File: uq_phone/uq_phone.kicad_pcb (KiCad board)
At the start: 4 copper layers, 116.9 x 105 mm, 304 parts, among them J1 USB4105-GF-A, J10 SJ-3551B-MSMT-TR-67, J11 Conn_01x02, J2 S3B-PH-SM4-TB_LF__SN_, J3 20279-001E-03, J4 20279-001E-03, J6 Conn_ARM_SWD_TagConnect_TC2030, J7 Conn_01x02, J8 KP15B-6S-SF_800_, J9 541324562, M1 VCDM0834B004L, Q1 MMBT3904LP-7, Q2 MMBT3904LP-7, SW1 SKTAAAE010, SW10 SKTAAAE010, SW11 SKTAAAE010, SW12 SKTAAAE010, SW13 SKTAAAE010, SW14 SKTAAAE010, SW15 SKTAAAE010, SW16 SKTAAAE010, SW17 SKTAAAE010, SW18 SKTAAAE010, SW19 SKTAAAE010, SW2 SKTAAAE010, SW20 SKTAAAE010, SW21 SKTAAAE010, SW22 SKTAAAE010, SW23 SKTAAAE010, SW24 SKTAAAE010, SW25 SKTAAAE010, SW26 SKTAAAE010, SW27 SKTAAAE010, SW28 SKTAAAE010, SW29 SKTAAAE010, SW3 SKTAAAE010, SW30 SKTAAAE010, SW31 SKTAAAE010, SW32 SKTAAAE010, SW33 SKTAAAE010, SW34 SKTAAAE010, SW35 SKTAAAE010, SW36 SKTAAAE010, SW37 SKTAAAE010, SW38 SKTAAAE010, SW39 SKTAAAE010, SW4 SKTAAAE010, SW40 SKTAAAE010, SW41 SKTAAAE010, SW42 SKTAAAE010, SW43 SKSCLCE010, SW44 SKSCLCE010, SW45 SKSCLCE010, SW46 SKSCLCE010, SW5 SKTAAAE010, SW6 SKTAAAE010, SW7 SKTAAAE010, SW8 SKTAAAE010, SW9 SKTAAAE010, U1 MCP73871-2CCI_ML, U10 TPD3F303DQDR, U11 TPD8F003DQDR, U12 MCP1664T-E/OT, U13 TS3A5018RSVR, U14 NAU88C22YG, U2 TPS62162DSGR, U3 BQ27441DRZR-G1A, U4 RC7620_1104625, U5 TXB0108RGYR, U6 TXB0108RGYR, U7 STM32H730VBTx, U8 LSM6DSVTR, U9 DRV2603RUNR

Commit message: Update Keypad
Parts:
- removed the LED13 at (137.1, 131.7)
- removed the LED13 at (169.8, 167.5)
- removed the LED13 at (180.2, 146.2)
- removed the LED13 at (137.1, 123.4)
- removed the LED13 at (155.3, 130.7)
- removed the LED13 at (158.5, 167.5)
- removed the LED13 at (180.2, 153.5)
- removed the LED13 at (124.0, 126.8)
- removed the LED13 at (180.2, 167.5)
- removed the LED13 at (170.2, 134.5)
- removed the LED13 at (183.3, 138.7)
- removed the LED13 at (158.5, 160.2)
- removed the LED13 at (137.2, 165.9)
- removed the LED13 at (109.3, 123.2)
- removed the LED13 at (155.3, 138.9)
- removed the LED13 at (169.8, 160.2)
- removed the LED13 at (183.3, 130.4)
- removed the LED13 at (169.8, 153.5)
- removed the LED13 at (158.5, 153.5)
- removed the LED13 at (169.8, 146.2)
- removed the LED13 at (109.3, 131.4)
- removed the LED13 at (180.2, 160.2)
- removed the LED13 at (158.5, 146.2)
- removed the REF** at (110.5, 157.0)
- removed the REF** at (124.0, 165.5)
- removed the REF** at (137.5, 140.0)
- removed the REF** at (137.5, 165.5)
- removed the REF** at (124.0, 157.0)
- removed the REF** at (110.5, 148.5)
- removed the REF** at (124.0, 148.4)
- removed the REF** at (124.0, 140.0)
- removed the REF** at (110.5, 140.0)
- removed the REF** at (137.5, 148.4)
- removed the REF** at (110.5, 165.5)
- removed the REF** at (137.5, 157.0)
- removed SW26, SW28, SW30, SW32: SKTAAAE010, custom_footprints:SKTAAAE010
- removed the SW36 at (174.2, 141.0)
- removed the SW36 at (136.2, 132.8)
- removed the SW36 at (169.3, 140.9)
- removed the SW36 at (179.4, 157.6)
- removed the SW36 at (136.2, 129.0)
- removed the SW36 at (136.2, 124.5)
- removed the SW36 at (108.5, 132.5)
- removed the SW36 at (128.0, 133.3)
- removed the SW36 at (179.4, 161.3)
- removed the SW36 at (179.4, 164.8)
- removed the SW36 at (176.3, 133.6)
- removed the SW36 at (164.0, 133.5)
- removed the SW36 at (123.0, 128.0)
- removed the SW36 at (169.2, 135.6)
- removed the SW36 at (108.5, 120.5)
- removed the SW36 at (157.7, 154.6)
- removed the SW36 at (179.4, 143.6)
- removed the SW36 at (117.8, 125.8)
- removed the SW36 at (168.9, 154.6)
- removed the SW36 at (169.2, 131.8)
- removed the SW36 at (123.0, 133.2)
- removed the SW36 at (157.7, 143.6)
- removed the SW36 at (154.5, 131.8)
- removed the SW36 at (179.4, 147.3)
- removed the SW36 at (154.5, 136.2)
- removed the SW36 at (154.5, 128.0)
- removed the SW36 at (157.7, 147.3)
- removed the SW36 at (108.5, 128.8)
- removed the SW36 at (127.5, 120.8)
- removed the SW36 at (123.0, 120.8)
- removed the SW36 at (168.9, 161.3)
- removed the SW36 at (182.5, 136.0)
- removed the SW36 at (234.2, 138.1)
- removed the SW36 at (157.7, 168.6)
- removed the SW36 at (157.7, 164.8)
- removed the SW36 at (157.7, 150.8)
- removed the SW36 at (108.5, 124.2)
- removed the SW36 at (179.4, 150.8)
- removed the SW36 at (136.2, 120.8)
- removed the SW36 at (157.7, 157.6)
- removed the SW36 at (179.4, 168.6)
- removed the SW36 at (130.1, 125.9)
- removed the SW36 at (168.9, 150.8)
- removed the SW36 at (168.9, 164.8)
- removed the SW36 at (168.9, 147.3)
- removed the SW36 at (163.8, 138.1)
- removed the SW36 at (169.3, 128.4)
- removed the SW36 at (179.4, 154.6)
- removed the SW36 at (130.1, 130.2)
- removed the SW36 at (123.0, 124.2)
- removed the SW36 at (182.5, 127.8)
- removed the SW36 at (176.3, 137.8)
- removed the SW36 at (168.9, 157.6)
- removed the SW36 at (154.5, 140.0)
- removed the SW36 at (157.7, 161.3)
- removed the SW36 at (117.6, 130.4)
- removed the SW36 at (168.9, 143.6)
- removed the SW36 at (173.8, 128.4)
- removed the SW36 at (182.5, 131.5)
- removed the SW36 at (168.9, 168.6)
- removed the SW36 at (182.5, 139.8)
- removed SW46: SKSCLCE010, custom_footprints:SKSCLCE010
- added REF**: 8.5mmSnaptron, custom_footprints:8.5mmSnaptron, F.Cu at (160.4, 143.4)
- added REF**: 8.5mmSnaptron, custom_footprints:8.5mmSnaptron, F.Cu at (127.5, 143.4)
- added REF**: 8.5mmSnaptron, custom_footprints:8.5mmSnaptron, F.Cu at (127.5, 159.4)
- added REF**: 8.5mmSnaptron, custom_footprints:8.5mmSnaptron, F.Cu at (127.5, 167.4)
- added REF**: 8.5mmSnaptron, custom_footprints:8.5mmSnaptron, F.Cu at (160.4, 167.4)
- added REF**: 8.5mmSnaptron, custom_footprints:8.5mmSnaptron, F.Cu at (160.4, 159.4)
- added REF**: 8.5mmSnaptron, custom_footprints:8.5mmSnaptron, F.Cu at (144.6, 167.4)
- added REF**: 8.5mmSnaptron, custom_footprints:8.5mmSnaptron, F.Cu at (144.6, 151.4)
- added REF**: 8.5mmSnaptron, custom_footprints:8.5mmSnaptron, F.Cu at (144.6, 159.4)
- added REF**: 8.5mmSnaptron, custom_footprints:8.5mmSnaptron, F.Cu at (144.6, 143.4)
- added REF**: 8.5mmSnaptron, custom_footprints:8.5mmSnaptron, F.Cu at (160.4, 151.4)
- added REF**: 8.5mmSnaptron, custom_footprints:8.5mmSnaptron, F.Cu at (127.5, 151.4)
- added SW36: SKTAAAE010, custom_footprints:SKTAAAE010, F.Cu at (81.3, 132.8)
- moved SW40 157.9 mm to (81.3, 139.8)
- moved SW39 157.7 mm to (81.3, 135.8)
- moved SW35 151.2 mm to (81.3, 128.8)
- moved SW8 148.1 mm to (83.3, 161.6)
- moved R48 146.0 mm to (67.1, 128.4), turned to -90 degrees
- moved SW2 145.5 mm to (83.3, 168.6)
- moved SW1 145.1 mm to (83.3, 164.6)
- moved SW20 143.1 mm to (83.3, 147.6)
- moved SW19 142.9 mm to (83.3, 143.6)
- moved SW31 141.0 mm to (95.3, 140.4)
- moved SW22 140.4 mm to (95.3, 147.6)
- moved SW25 140.0 mm to (90.0, 135.9), turned to 90 degrees
- moved SW14 139.4 mm to (83.3, 154.6)
- moved SW13 139.2 mm to (83.3, 150.6)
- moved SW34 138.4 mm to (95.3, 136.2)
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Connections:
- SW1 pad 1: Net-(SW1-Pad1) -> PB_STAR
- SW1 pad 2: Net-(SW1-Pad2) -> GND
- SW1 pad 3: Net-(SW1-Pad1) -> PB_STAR
- SW1 pad 4: Net-(SW1-Pad2) -> GND
- SW10 pad 1: Net-(SW10-Pad1) -> PB_2
- SW10 pad 2: Net-(SW10-Pad2) -> GND
- SW10 pad 3: Net-(SW10-Pad1) -> PB_2
- SW10 pad 4: Net-(SW10-Pad2) -> GND
- SW11 pad 1: Net-(SW11-Pad1) -> PB_3
- SW11 pad 2: Net-(SW11-Pad2) -> GND
- SW11 pad 3: Net-(SW11-Pad1) -> PB_3
- SW11 pad 4: Net-(SW11-Pad2) -> GND
- SW12 pad 1: Net-(SW11-Pad1) -> PB_3
- SW12 pad 2: Net-(SW11-Pad2) -> GND
- SW12 pad 3: Net-(SW11-Pad1) -> PB_3
- SW12 pad 4: Net-(SW11-Pad2) -> GND
- SW13 pad 1: Net-(SW13-Pad1) -> PB_4
- SW13 pad 2: Net-(SW13-Pad2) -> GND
- SW13 pad 3: Net-(SW13-Pad1) -> PB_4
- SW13 pad 4: Net-(SW13-Pad2) -> GND
- SW14 pad 1: Net-(SW13-Pad1) -> PB_4
- SW14 pad 2: Net-(SW13-Pad2) -> GND
- SW14 pad 3: Net-(SW13-Pad1) -> PB_4
- SW14 pad 4: Net-(SW13-Pad2) -> GND
- SW15 pad 1: Net-(SW15-Pad1) -> PB_5
- SW15 pad 2: Net-(SW15-Pad2) -> GND
- SW15 pad 3: Net-(SW15-Pad1) -> PB_5
- SW15 pad 4: Net-(SW15-Pad2) -> GND
- SW16 pad 1: Net-(SW15-Pad1) -> PB_5
- SW16 pad 2: Net-(SW15-Pad2) -> GND
- SW16 pad 3: Net-(SW15-Pad1) -> PB_5
- SW16 pad 4: Net-(SW15-Pad2) -> GND
- SW17 pad 1: Net-(SW17-Pad1) -> PB_6
- SW17 pad 2: Net-(SW17-Pad2) -> GND
- SW17 pad 3: Net-(SW17-Pad1) -> PB_6
- SW17 pad 4: Net-(SW17-Pad2) -> GND
- SW18 pad 1: Net-(SW17-Pad1) -> PB_6
- SW18 pad 2: Net-(SW17-Pad2) -> GND
- SW18 pad 3: Net-(SW17-Pad1) -> PB_6
- SW18 pad 4: Net-(SW17-Pad2) -> GND
- SW19 pad 1: Net-(SW19-Pad1) -> PB_7
- SW19 pad 2: Net-(SW19-Pad2) -> GND
- SW19 pad 3: Net-(SW19-Pad1) -> PB_7
- SW19 pad 4: Net-(SW19-Pad2) -> GND
- SW2 pad 1: Net-(SW1-Pad1) -> PB_STAR
- SW2 pad 2: Net-(SW1-Pad2) -> GND
- SW2 pad 3: Net-(SW1-Pad1) -> PB_STAR
- SW2 pad 4: Net-(SW1-Pad2) -> GND
- SW20 pad 1: Net-(SW19-Pad1) -> PB_7
- SW20 pad 2: Net-(SW19-Pad2) -> GND
- SW20 pad 3: Net-(SW19-Pad1) -> PB_7
- SW20 pad 4: Net-(SW19-Pad2) -> GND
- SW21 pad 1: Net-(SW21-Pad1) -> PB_8
- SW21 pad 2: Net-(SW21-Pad2) -> GND
- SW21 pad 3: Net-(SW21-Pad1) -> PB_8
- SW21 pad 4: Net-(SW21-Pad2) -> GND
- SW22 pad 1: Net-(SW21-Pad1) -> PB_8
- SW22 pad 2: Net-(SW21-Pad2) -> GND
- SW22 pad 3: Net-(SW21-Pad1) -> PB_8
- SW22 pad 4: Net-(SW21-Pad2) -> GND
- SW23 pad 1: Net-(SW23-Pad1) -> PB_9
- SW23 pad 2: Net-(SW23-Pad2) -> GND
- SW23 pad 3: Net-(SW23-Pad1) -> PB_9
- SW23 pad 4: Net-(SW23-Pad2) -> GND
- SW24 pad 1: Net-(SW23-Pad1) -> PB_9
- SW24 pad 2: Net-(SW23-Pad2) -> GND
- SW24 pad 3: Net-(SW23-Pad1) -> PB_9
- SW24 pad 4: Net-(SW23-Pad2) -> GND
- SW25 pad 1: Net-(SW25-Pad1) -> PB_DPAD_LEFT
- SW25 pad 2: Net-(SW25-Pad2) -> GND
- SW25 pad 3: Net-(SW25-Pad1) -> PB_DPAD_LEFT
- SW25 pad 4: Net-(SW25-Pad2) -> GND
- SW27 pad 1: Net-(SW27-Pad1) -> PB_DPAD_UP
- SW27 pad 2: Net-(SW27-Pad2) -> GND
- SW27 pad 3: Net-(SW27-Pad1) -> PB_DPAD_UP
- SW27 pad 4: Net-(SW27-Pad2) -> GND
- SW29 pad 1: Net-(SW29-Pad1) -> PB_DPAD_RIGHT
- SW29 pad 2: Net-(SW29-Pad2) -> GND
- SW29 pad 3: Net-(SW29-Pad1) -> PB_DPAD_RIGHT
- SW29 pad 4: Net-(SW29-Pad2) -> GND
- SW3 pad 1: Net-(SW3-Pad1) -> PB_0
- SW3 pad 2: Net-(SW3-Pad2) -> GND
- SW3 pad 3: Net-(SW3-Pad1) -> PB_0
- SW3 pad 4: Net-(SW3-Pad2) -> GND
- SW31 pad 1: Net-(SW31-Pad1) -> PB_DPAD_DOWN
- SW31 pad 2: Net-(SW31-Pad2) -> GND
- SW31 pad 3: Net-(SW31-Pad1) -> PB_DPAD_DOWN
- SW31 pad 4: Net-(SW31-Pad2) -> GND
- SW33 pad 1: Net-(SW33-Pad1) -> PB_DPAD_SELECT
- SW33 pad 2: Net-(SW33-Pad2) -> GND
- SW33 pad 3: Net-(SW33-Pad1) -> PB_DPAD_SELECT
- SW33 pad 4: Net-(SW33-Pad2) -> GND
- SW34 pad 1: Net-(SW33-Pad1) -> PB_DPAD_SELECT
- SW34 pad 2: Net-(SW33-Pad2) -> GND
- SW34 pad 3: Net-(SW33-Pad1) -> PB_DPAD_SELECT
- SW34 pad 4: Net-(SW33-Pad2) -> GND
- SW35 pad 1: Net-(SW35-Pad1) -> PB_MENU_L
- SW35 pad 2: Net-(SW35-Pad2) -> GND
- SW35 pad 3: Net-(SW35-Pad1) -> PB_MENU_L
- SW35 pad 4: Net-(SW35-Pad2) -> GND
- SW37 pad 1: Net-(SW37-Pad1) -> PB_MENU_R
- SW37 pad 2: Net-(SW37-Pad2) -> GND
- SW37 pad 3: Net-(SW37-Pad1) -> PB_MENU_R
- SW37 pad 4: Net-(SW37-Pad2) -> GND
- SW38 pad 1: Net-(SW37-Pad1) -> PB_MENU_R
- SW38 pad 2: Net-(SW37-Pad2) -> GND
- SW38 pad 3: Net-(SW37-Pad1) -> PB_MENU_R
- SW38 pad 4: Net-(SW37-Pad2) -> GND
- SW39 pad 1: Net-(SW39-Pad1) -> PB_CALL
- SW39 pad 2: Net-(SW39-Pad2) -> GND
- SW39 pad 3: Net-(SW39-Pad1) -> PB_CALL
- SW39 pad 4: Net-(SW39-Pad2) -> GND
- SW4 pad 1: Net-(SW3-Pad1) -> PB_0
- SW4 pad 2: Net-(SW3-Pad2) -> GND
- SW4 pad 3: Net-(SW3-Pad1) -> PB_0
- SW4 pad 4: Net-(SW3-Pad2) -> GND
- SW40 pad 1: Net-(SW39-Pad1) -> PB_CALL
- SW40 pad 2: Net-(SW39-Pad2) -> GND
- SW40 pad 3: Net-(SW39-Pad1) -> PB_CALL
- SW40 pad 4: Net-(SW39-Pad2) -> GND
- SW41 pad 1: Net-(SW41-Pad1) -> PB_END_CALL
- SW41 pad 2: Net-(SW41-Pad2) -> GND
- SW41 pad 3: Net-(SW41-Pad1) -> PB_END_CALL
- SW41 pad 4: Net-(SW41-Pad2) -> GND
- SW42 pad 1: Net-(SW41-Pad1) -> PB_END_CALL
- SW42 pad 2: Net-(SW41-Pad2) -> GND
- SW42 pad 3: Net-(SW41-Pad1) -> PB_END_CALL
- SW42 pad 4: Net-(SW41-Pad2) -> GND
- SW43 pad 1: unconnected-(SW43-Pad1) -> PB_VOL_UP
- SW43 pad 2: unconnected-(SW43-Pad2) -> PB_VOL_UP
- SW43 pad 3: unconnected-(SW43-Pad3) -> GND
- SW43 pad 4: unconnected-(SW43-Pad4) -> GND
- SW44 pad 1: unconnected-(SW44-Pad1) -> PB_PWR
- SW44 pad 2: unconnected-(SW44-Pad2) -> PB_PWR
- SW44 pad 3: unconnected-(SW44-Pad3) -> GND
- SW44 pad 4: unconnected-(SW44-Pad4) -> GND
- SW45 pad 1: unconnected-(SW45-Pad1) -> PB_VOL_DOWN
- SW45 pad 2: unconnected-(SW45-Pad2) -> PB_VOL_DOWN
- SW45 pad 3: unconnected-(SW45-Pad3) -> GND
- SW45 pad 4: unconnected-(SW45-Pad4) -> GND
- SW5 pad 1: Net-(SW5-Pad1) -> PB_HASH
- SW5 pad 2: Net-(SW5-Pad2) -> GND
- SW5 pad 3: Net-(SW5-Pad1) -> PB_HASH
- SW5 pad 4: Net-(SW5-Pad2) -> GND
- SW6 pad 1: Net-(SW5-Pad1) -> PB_HASH
- SW6 pad 2: Net-(SW5-Pad2) -> GND
- SW6 pad 3: Net-(SW5-Pad1) -> PB_HASH
- SW6 pad 4: Net-(SW5-Pad2) -> GND
- SW7 pad 1: Net-(SW7-Pad1) -> PB_1
- SW7 pad 2: Net-(SW7-Pad2) -> GND
- SW7 pad 3: Net-(SW7-Pad1) -> PB_1
- SW7 pad 4: Net-(SW7-Pad2) -> GND
- SW8 pad 1: Net-(SW7-Pad1) -> PB_1
- SW8 pad 2: Net-(SW7-Pad2) -> GND
- SW8 pad 3: Net-(SW7-Pad1) -> PB_1
- SW8 pad 4: Net-(SW7-Pad2) -> GND
- SW9 pad 1: Net-(SW10-Pad1) -> PB_2
- SW9 pad 2: Net-(SW10-Pad2) -> GND
- SW9 pad 3: Net-(SW10-Pad1) -> PB_2
- SW9 pad 4: Net-(SW10-Pad2) -> GND
- U7 pad 1: unconnected-(U7-PE2-Pad1) -> PB_HASH
- U7 pad 12: unconnected-(U7-PH0-Pad12) -> PB_8
- U7 pad 13: unconnected-(U7-PH1-Pad13) -> PB_9
- U7 pad 15: unconnected-(U7-PC0-Pad15) -> PB_MENU_L
- U7 pad 16: unconnected-(U7-PC1-Pad16) -> PB_MENU_R
- U7 pad 2: unconnected-(U7-PE3-Pad2) -> PB_1
- U7 pad 22: unconnected-(U7-PA0-Pad22) -> PB_PWR
- U7 pad 23: unconnected-(U7-PA1-Pad23) -> PB_VOL_DOWN
- U7 pad 24: unconnected-(U7-PA2-Pad24) -> PB_VOL_UP
- U7 pad 25: unconnected-(U7-PA3-Pad25) -> LED_DATA
- U7 pad 3: unconnected-(U7-PE4-Pad3) -> PB_2
- U7 pad 4: unconnected-(U7-PE5-Pad4) -> PB_3
- U7 pad 5: unconnected-(U7-PE6-Pad5) -> PB_4
- U7 pad 7: unconnected-(U7-PC13-Pad7) -> PB_5
- U7 pad 77: unconnected-(U7-PA15(JTDI)-Pad77) -> PB_END_CALL
- U7 pad 8: unconnected-(U7-PC14-Pad8) -> PB_6
- U7 pad 87: unconnected-(U7-PD6-Pad87) -> PB_CALL
- U7 pad 89: unconnected-(U7-PB3(JTDO-Pad89) -> PB_DPAD_UP
- U7 pad 9: unconnected-(U7-PC15-Pad9) -> PB_7
- U7 pad 90: unconnected-(U7-PB4(NJTRST)-Pad90) -> PB_DPAD_DOWN
- U7 pad 91: unconnected-(U7-PB5-Pad91) -> PB_DPAD_RIGHT
- U7 pad 92: unconnected-(U7-PB6-Pad92) -> PB_DPAD_LEFT
- U7 pad 93: unconnected-(U7-PB7-Pad93) -> PB_DPAD_SELECT
- U7 pad 97: unconnected-(U7-PE0-Pad97) -> PB_STAR
- U7 pad 98: unconnected-(U7-PE1-Pad98) -> PB_0
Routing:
- net (no net): track 9.00 -> 0.00 mm
- net PB_STAR: track 0.00 -> 1.50 mm
- net PB_MENU_R: track 0.00 -> 1.50 mm
- net PB_MENU_L: track 0.00 -> 1.50 mm
- net PB_HASH: track 0.00 -> 1.50 mm
- net PB_END_CALL: track 0.00 -> 1.50 mm
- net PB_DPAD_SELECT: track 0.00 -> 1.50 mm
- net PB_CALL: track 0.00 -> 1.50 mm
- net PB_9: track 0.00 -> 1.50 mm
- net PB_8: track 0.00 -> 1.50 mm
- net PB_7: track 0.00 -> 1.50 mm
- net PB_6: track 0.00 -> 1.50 mm
- net PB_5: track 0.00 -> 1.50 mm
- net PB_4: track 0.00 -> 1.50 mm
- net PB_3: track 0.00 -> 1.50 mm
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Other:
- board size 116.9 x 105 mm -> 138 x 104.1 mm
- board text added: "LEFT"
- board text added: "RIGHT"

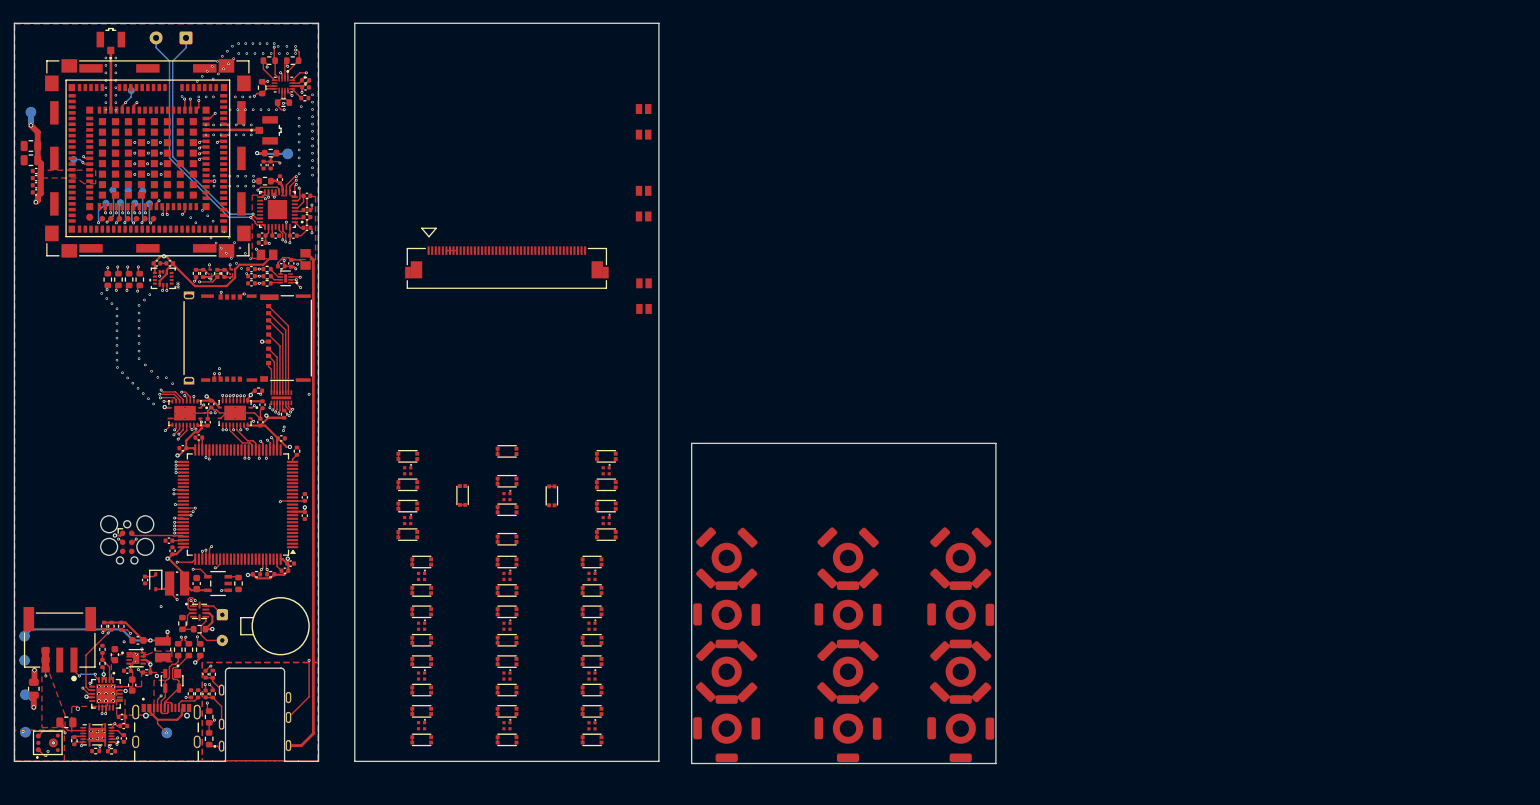
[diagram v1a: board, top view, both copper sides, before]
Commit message: Add Front Pannel Suboard and connector
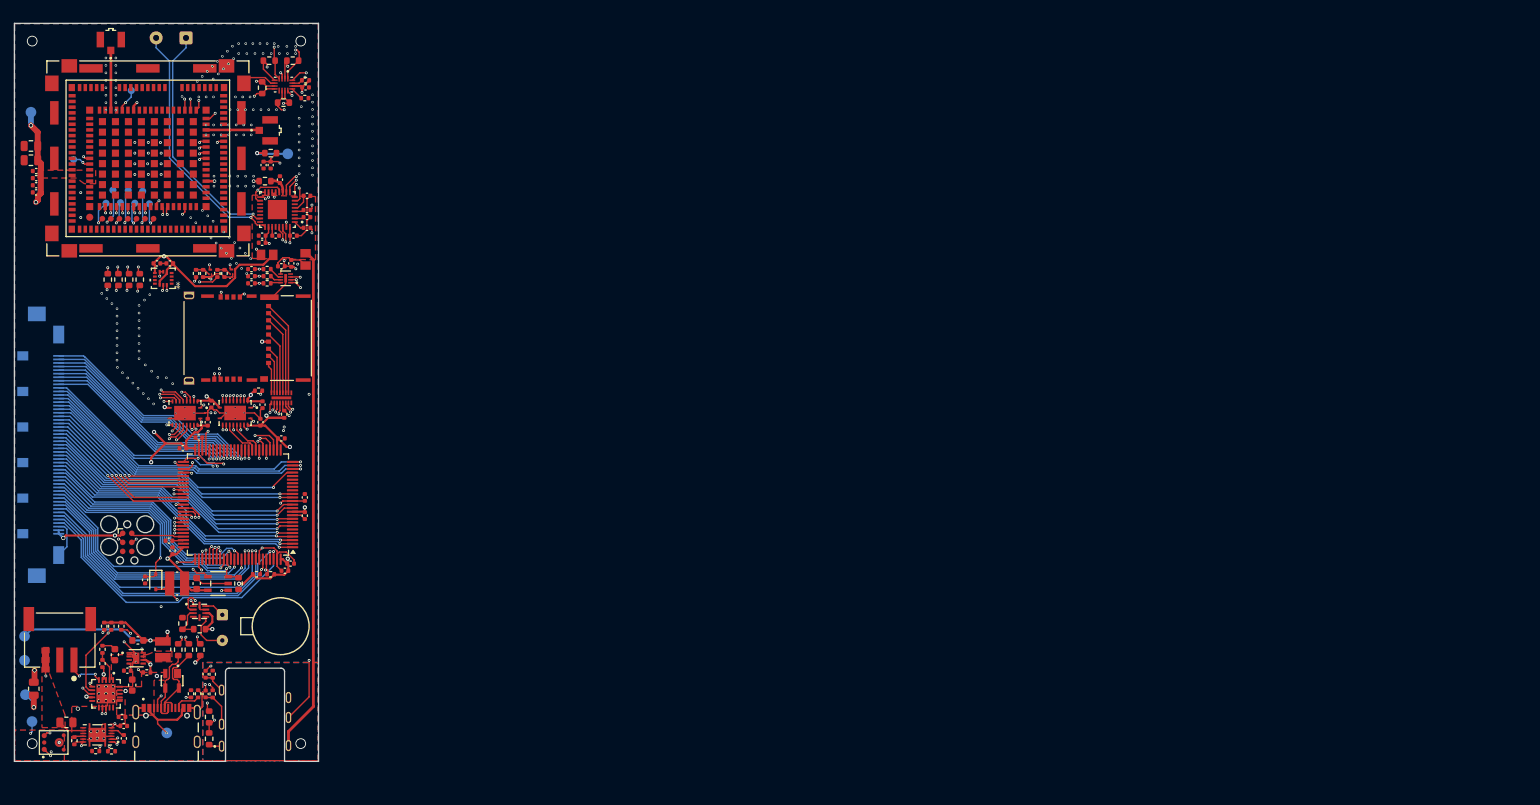
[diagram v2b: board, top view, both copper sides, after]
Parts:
- removed J9: 541324562, 541324562:CON_541324562_MOL
- removed LED1, LED10, LED11, LED12, LED13, LED14, LED15, LED16, LED17, LED2, LED3, LED4, LED5, LED6, LED7, LED8, LED9: XL-1010RGBC, custom_footprints:XL-1010RGBC-WS2812B
- removed R48: 330R, Resistor_SMD:R_0402_1005Metric
- removed REF** (x12): 8.5mmSnaptron, custom_footprints:8.5mmSnaptron
- removed SW1, SW10, SW11, SW12, SW13, SW14, SW15, SW16, SW17, SW18, SW19, SW2, SW20, SW21, SW22, SW23, SW24, SW25, SW27, SW29, SW3, SW31, SW33, SW34, SW35, SW36, SW37, SW38, SW39, SW4, SW40, SW41, SW42, SW5, SW6, SW7, SW8, SW9: SKTAAAE010, custom_footprints:SKTAAAE010
- removed SW43, SW44, SW45: SKSCLCE010, custom_footprints:SKSCLCE010
- added J5: FI-RE51S-HF-R1500, FI-RE51S-HF-R1500:JAE_FI-RE51S-HF-R1500, B.Cu at (33.6, 127.5)
- moved TP4 1.76 mm to (29.9, 166.4)
- moved MK1 0.83 mm to (32.9, 169.3)
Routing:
- net GND: track 37.6 -> 89.4 mm, vias 171 -> 182
- net DISP_DB3: track 0.00 -> 40.1 mm, vias 0 -> 2
- net PB_0: track 1.50 -> 41.5 mm, vias 0 -> 1
- net PB_VOL_UP: track 0.00 -> 39.7 mm, vias 0 -> 1
- net PB_VOL_DOWN: track 0.00 -> 39.5 mm, vias 0 -> 1
- net DISP_DB2: track 0.00 -> 39.4 mm, vias 0 -> 2
- net PB_STAR: track 1.50 -> 40.2 mm, vias 0 -> 1
- net PB_PWR: track 0.00 -> 38.6 mm, vias 0 -> 1
- net LED_DATA: track 1.25 -> 39.8 mm, vias 0 -> 1
- net PB_DPAD_SELECT: track 1.50 -> 39.4 mm, vias 0 -> 1
- net PB_DPAD_LEFT: track 0.75 -> 38.5 mm, vias 0 -> 1
- net PB_3: track 1.50 -> 37.9 mm, vias 0 -> 1
- net PB_MENU_R: track 1.50 -> 37.8 mm, vias 0 -> 1
- net PB_MENU_L: track 1.50 -> 37.8 mm, vias 0 -> 1
- net PB_8: track 1.50 -> 37.6 mm, vias 0 -> 1
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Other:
- board size 138 x 104.1 mm -> 42.8 x 103.8 mm

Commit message: Change MCU to h733VG
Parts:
- U7: value STM32H730VBTx -> STM32H733VGTx
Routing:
- net DISP_LEDA: track 25.2 -> 21.9 mm, vias 1 -> 2
- net GND: track 89.4 -> 91.0 mm, vias 182 -> 183
- net DISP_LEDK: track 32.9 -> 34.4 mm, vias 1 -> 3
- net PB_DPAD_RIGHT: track 36.8 -> 38.0 mm, vias 1 -> 3
- net PB_END_CALL: track 28.0 -> 29.2 mm, vias 1 -> 3
- net PB_STAR: track 40.2 -> 41.4 mm, vias 1 -> 3
- net PB_DPAD_DOWN: track 36.3 -> 37.4 mm, vias 1 -> 3
- net +3.3V: track 248.2 -> 247.1 mm
- net PB_DPAD_LEFT: track 38.5 -> 39.5 mm, vias 1 -> 3
- net DISP_RES: track 30.7 -> 31.7 mm, vias 1 -> 3
- net PB_DPAD_UP: track 33.4 -> 34.3 mm, vias 1 -> 3
- net DISP_RD: track 32.0 -> 32.9 mm, vias 1 -> 3
- net PB_CALL: track 32.3 -> 33.1 mm, vias 1 -> 3
- net PB_DPAD_SELECT: track 39.4 -> 40.2 mm, vias 1 -> 3
- net DISP_DB1: track 21.4 -> 22.2 mm, vias 1 -> 2
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
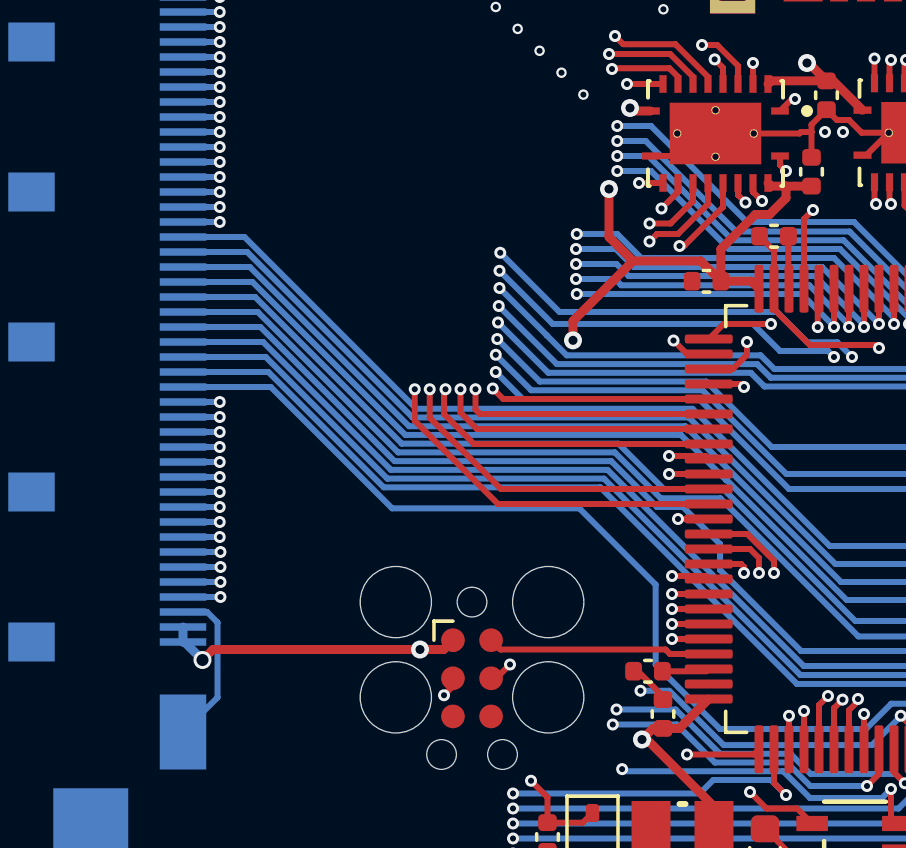
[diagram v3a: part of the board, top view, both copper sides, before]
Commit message: Swap RX TX
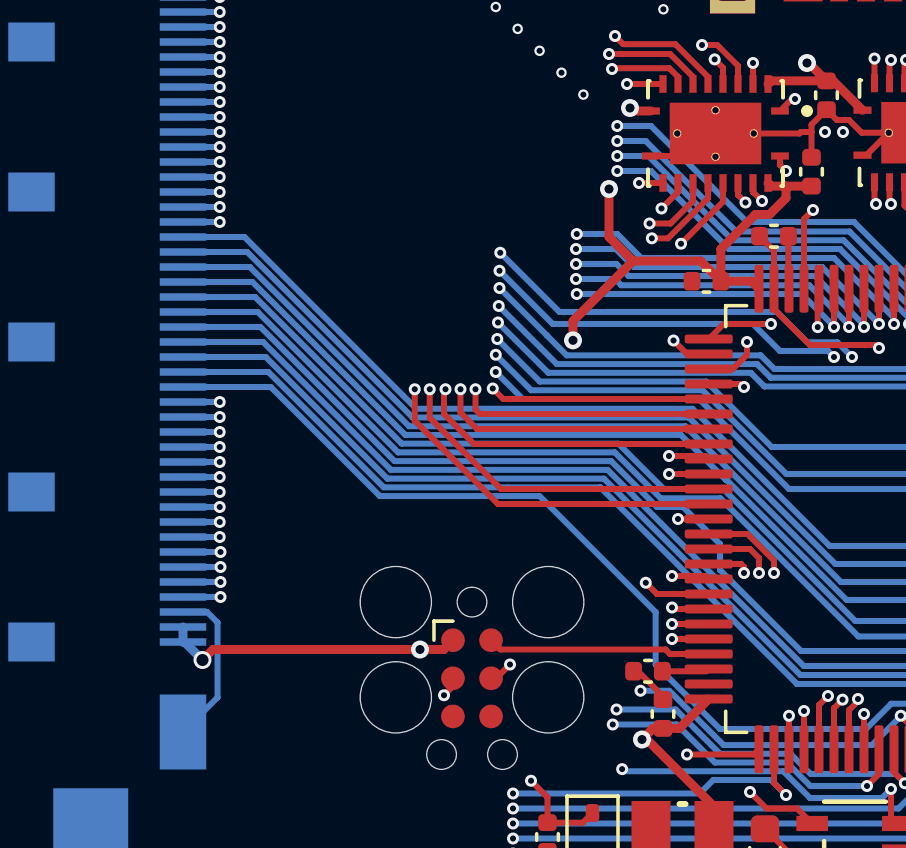
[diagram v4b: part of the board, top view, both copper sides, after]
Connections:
- U7 pad 68: MCU_RXD -> MCU_TXD
- U7 pad 69: MCU_TXD -> MCU_RXD
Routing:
- net DISP_CS: track 32.9 -> 32.4 mm
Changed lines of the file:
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@@
 			(layers "F.Cu" "F.Mask" "F.Paste")
 			(roundrect_rratio 0.25)
-			(net 87 "MCU_RXD")
+			(net 88 "MCU_TXD")
 			(pinfunction "PA9")
 			(pintype "bidirectional")
@@
 			(layers "F.Cu" "F.Mask" "F.Paste")
 			(roundrect_rratio 0.25)
-			(net 88 "MCU_TXD")
+			(net 87 "MCU_RXD")
 			(pinfunction "PA10")
 			(pintype "bidirectional")
@@
 	)
 	(segment
-		(start 58.3 142.4)
-		(end 57.957115 142.057115)
+		(start 57.209985 142.057115)
+		(end 56.3671 142.9)
+		(width 0.2)
+		(layer "B.Cu")
+		(net 50)
+	)
+	(segment
+		(start 40.169872 135.135232)
+		(end 40.15964 135.125)
 		(width 0.2)
 		(layer "B.Cu")
@@
 	)
 	(segment
-		(start 57.957115 142.057115)
-		(end 57.209985 142.057115)
+		(start 45.485232 135.135232)
+		(end 40.169872 135.135232)
 		(width 0.2)
 		(layer "B.Cu")
@@
 	)
 	(segment
-		(start 36.525 131.5)
-		(end 40.57 135.545)
+		(start 57.957115 142.057115)
+		(end 57.209985 142.057115)
 		(width 0.2)
 		(layer "B.Cu")
@@
 	)
 	(segment
-		(start 46.811666 135.545)
-		(end 40.57 135.545)
+		(start 58.3 142.4)
+		(end 57.957115 142.057115)
 		(width 0.2)
 		(layer "B.Cu")
@@
 	)
 	(segment
-		(start 57.209985 142.057115)
-		(end 56.3671 142.9)
+		(start 49.355 140.755)
+		(end 49.355 139.005)
 		(width 0.2)
 		(layer "B.Cu")
@@
 	)
 	(segment
-		(start 33.6 131.5)
+		(start 40.15 135.125)
 		(end 36.525 131.5)
 		(width 0.2)
@@
 	)
 	(segment
-		(start 49.355 138.088334)
-		(end 46.811666 135.545)
+		(start 40.15964 135.125)
+		(end 40.15 135.125)
 		(width 0.2)
 		(layer "B.Cu")
@@
 	)
 	(segment
-		(start 49.355 140.755)
-		(end 49.355 138.088334)
+		(start 49.355 139.005)
+		(end 45.485232 135.135232)
+		(width 0.2)
+		(layer "B.Cu")
+		(net 50)
+	)
+	(segment
+		(start 36.525 131.5)
+		(end 33.6 131.5)
 		(width 0.2)
 		(layer "B.Cu")
@@
 	)
 	(segment
-		(start 51.6 125.5)
-		(end 51.6 124.7)
+		(start 49.95 138.9)
+		(end 49.9 138.85)
 		(width 0.2)
 		(layer "F.Cu")
@@
 	)
 	(segment
-		(start 49.9 138.4)
-		(end 51.125 138.4)
+		(start 51.6 125.325)
+		(end 50.2 126.725)
 		(width 0.2)
 		(layer "F.Cu")
@@
 	)
 	(segment
-		(start 50.15 126.8)
-		(end 50.3 126.8)
+		(start 51.6 124.7)
+		(end 51.6 125.325)
 		(width 0.2)
 		(layer "F.Cu")
@@
 	)
 	(segment
-		(start 50.3 126.8)
-		(end 51.6 125.5)
+		(start 51.125 138.9)
+		(end 49.95 138.9)
 		(width 0.2)
 		(layer "F.Cu")
@@
 	)
 	(via
-		(at 50.15 126.8)
+		(at 49.9 138.85)
 		(size 0.4)
 		(drill 0.2)
@@
 	)
 	(via
-		(at 49.9 138.4)
+		(at 50.2 126.725)
 		(size 0.4)
 		(drill 0.2)
@@
 	)
 	(segment
-		(start 50.15 126.8)
-		(end 50.1 126.8)
+		(start 49.499 138.449)
+		(end 49.9 138.85)
 		(width 0.2)
 		(layer "In2.Cu")
@@
 	)
 	(segment
-		(start 48.664 137.164)
-		(end 49.9 138.4)
+		(start 49.499 137.924)
+		(end 49.499 138.449)
 		(width 0.2)
 		(layer "In2.Cu")
@@
 	)
 	(segment
-		(start 48.664 128.236)
-		(end 48.664 137.164)
+		(start 48.664 128.261)
+		(end 48.664 137.089)
 		(width 0.2)
 		(layer "In2.Cu")
@@
 	)
 	(segment
-		(start 50.1 126.8)
-		(end 48.664 128.236)
+		(start 50.2 126.725)
+		(end 48.664 128.261)
 		(width 0.2)
 		(layer "In2.Cu")
@@
 	)
 	(segment
-		(start 51.1 125.4)
-		(end 51.1 124.7)
+		(start 48.664 137.089)
+		(end 49.499 137.924)
+		(width 0.2)
+		(layer "In2.Cu")
+		(net 87)
+	)
+	(segment
+		(start 49.4 138.4)
+		(end 49.025 138.025)
 		(width 0.2)
 		(layer "F.Cu")
@@
 	)
 	(segment
-		(start 49.15 126.65)
-		(end 49.4 126.4)
+		(start 49.227982 126.543884)
+		(end 49.767652 126.543884)
 		(width 0.2)
 		(layer "F.Cu")
@@
 	)
 	(segment
-		(start 50.1 126.4)
-		(end 51.1 125.4)
+		(start 51.125 138.4)
+		(end 49.4 138.4)
 		(width 0.2)
 		(layer "F.Cu")
@@
 	)
 	(segment
-		(start 51.125 138.9)
-		(end 49.9 138.9)
+		(start 49.767652 126.543884)
+		(end 51.1 125.211536)
 		(width 0.2)
 		(layer "F.Cu")
@@
 	)
 	(segment
-		(start 49.4 126.4)
-		(end 50.1 126.4)
+		(start 51.1 125.211536)
+		(end 51.1 124.7)
 		(width 0.2)
 		(layer "F.Cu")
@@
 	)
 	(via
-		(at 49.15 126.65)
+		(at 49.025 138.025)
 		(size 0.4)
 		(drill 0.2)
@@
 	)
 	(via
-		(at 49.9 138.9)
+		(at 49.227982 126.543884)
 		(size 0.4)
 		(drill 0.2)
@@
 	)
 	(segment
-		(start 48.373 137.438686)
-		(end 49.834314 138.9)
-		(width 0.2)
-		(layer "In2.Cu")
-		(net 88)
-	)
-	(segment
-		(start 49.15 126.65)
-		(end 48.373 127.427)
+		(start 48.373 127.398866)
+		(end 49.227982 126.543884)
 		(width 0.2)
 		(layer "In2.Cu")
@@
 	)
 	(segment
-		(start 49.834314 138.9)
-		(end 49.9 138.9)
+		(start 49.025 138.025)
+		(end 48.373 137.373)
 		(width 0.2)
 		(layer "In2.Cu")
@@
 	)
 	(segment
-		(start 48.373 127.427)
-		(end 48.373 137.438686)
+		(start 48.373 137.373)
+		(end 48.373 127.398866)
 		(width 0.2)
 		(layer "In2.Cu")
